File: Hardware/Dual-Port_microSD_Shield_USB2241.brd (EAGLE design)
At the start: 22.9 x 58.4 mm, 85 parts, among them IC1 USB224X_2241, J2 MICRO-SD-PUSH-PUSH-EXT-PIN, J3 AVR_SPI_PROG_3X2TESTPOINTS, J4 THING_PLUS, Q1 20V/4.2A/52mΩ/1.4W, Q2 20V/0.2A/8MHz/1.2Ω/1Vth, Q3 20V/4.2A/52mΩ/1.4W, Q4 20V/4.2A/52mΩ/1.4W, Q6 20V/4.2A/52mΩ/1.4W, U1 3.3V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

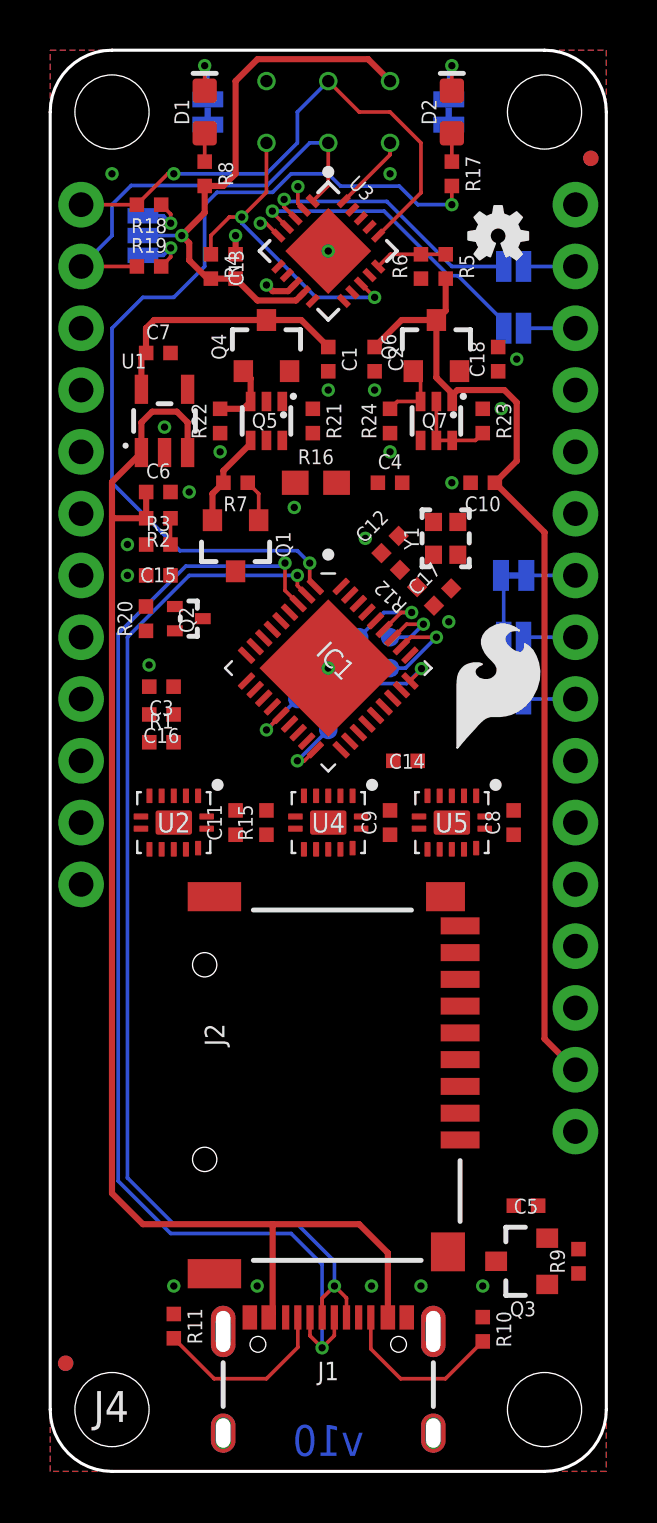
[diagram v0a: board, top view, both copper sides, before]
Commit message: Changed to 4-layer PCB. Routed. Add Schematic.pdf.
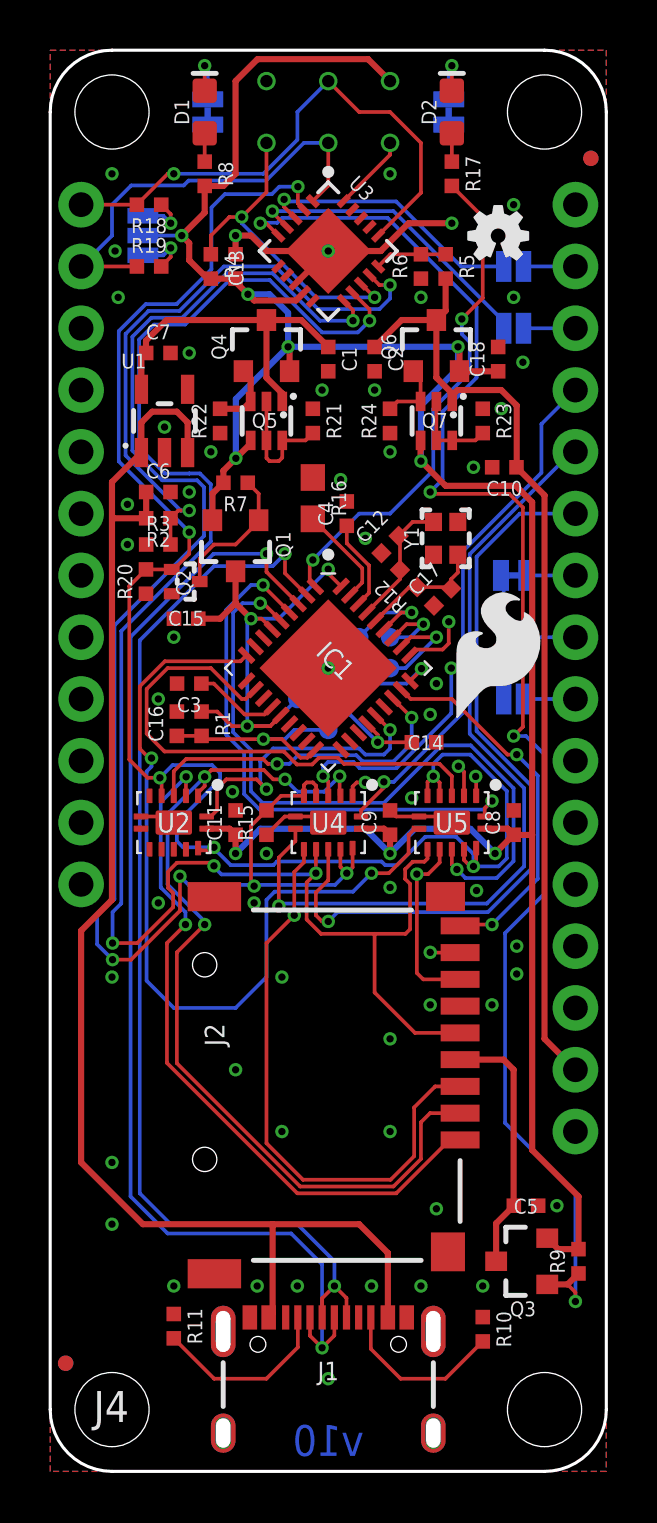
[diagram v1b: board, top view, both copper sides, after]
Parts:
- moved C4 2.18 mm to (12.2, 39.4), turned to 90 degrees
- moved C15 2.11 mm to (5.59, 35.1)
- moved R1 1.82 mm to (6.22, 30.7), turned to 270 degrees
- moved Q2 1.53 mm to (6.10, 36.6)
- moved R20 1.52 mm to (3.94, 36.6)
- moved LOGO4 1.27 mm to (18.4, 33.5)
- moved C3 1.15 mm to (5.71, 32.4)
- moved C10 1.09 mm to (18.7, 41.3)
- moved C14 1.08 mm to (15.4, 30.0)
- moved C16 0.74 mm to (5.21, 30.7), turned to 90 degrees
- moved R16 0.65 mm to (10.8, 40.0), turned to 270 degrees
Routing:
- net VCC: track 27.0 -> 110.6 mm, vias 1 -> 9
- net MICROSD_CLK/SCK: track 0.00 -> 71.0 mm, vias 0 -> 4
- net SDIO_EN: track 1.05 -> 68.5 mm, vias 1 -> 6
- net SPI_EN: track 0.00 -> 62.9 mm, vias 0 -> 5
- net MICROSD_PWR_EN: track 0.95 -> 61.7 mm, vias 1 -> 4
- net MICROSD_CMD/SDI: track 0.00 -> 38.1 mm, vias 0 -> 2
- net MICROSD_D3/!CS!: track 0.00 -> 37.4 mm, vias 0 -> 4
- net SD_CLK: track 0.00 -> 34.4 mm, vias 0 -> 2
- net PICO: track 0.00 -> 34.1 mm, vias 0 -> 1
- net SCLK: track 0.00 -> 31.3 mm, vias 0 -> 1
- net SD_D0: track 0.00 -> 29.5 mm, vias 0 -> 2
- net MICROSD_D2: track 0.00 -> 28.9 mm, vias 0 -> 2
- net SDIO_VDD: track 2.64 -> 27.1 mm, vias 1 -> 4
- net V_USB_DIV_2: track 1.08 -> 25.0 mm, vias 0 -> 2
- net SD_D1: track 0.00 -> 22.7 mm, vias 0 -> 2
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- added copper zone on layer 2, net GND
- added copper zone on layer 15, net VCC
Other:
- board text added: "4-Layer Board 1.6mm Thickness 1oz Copper (Outer layers) HASL Finish"
- board text removed: "2-Layer Board 1.6mm Thickness 1oz Copper (Outer layers) HASL Finish"

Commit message: Add silk. Replace xtal caps with calculated values. Finishing touches...
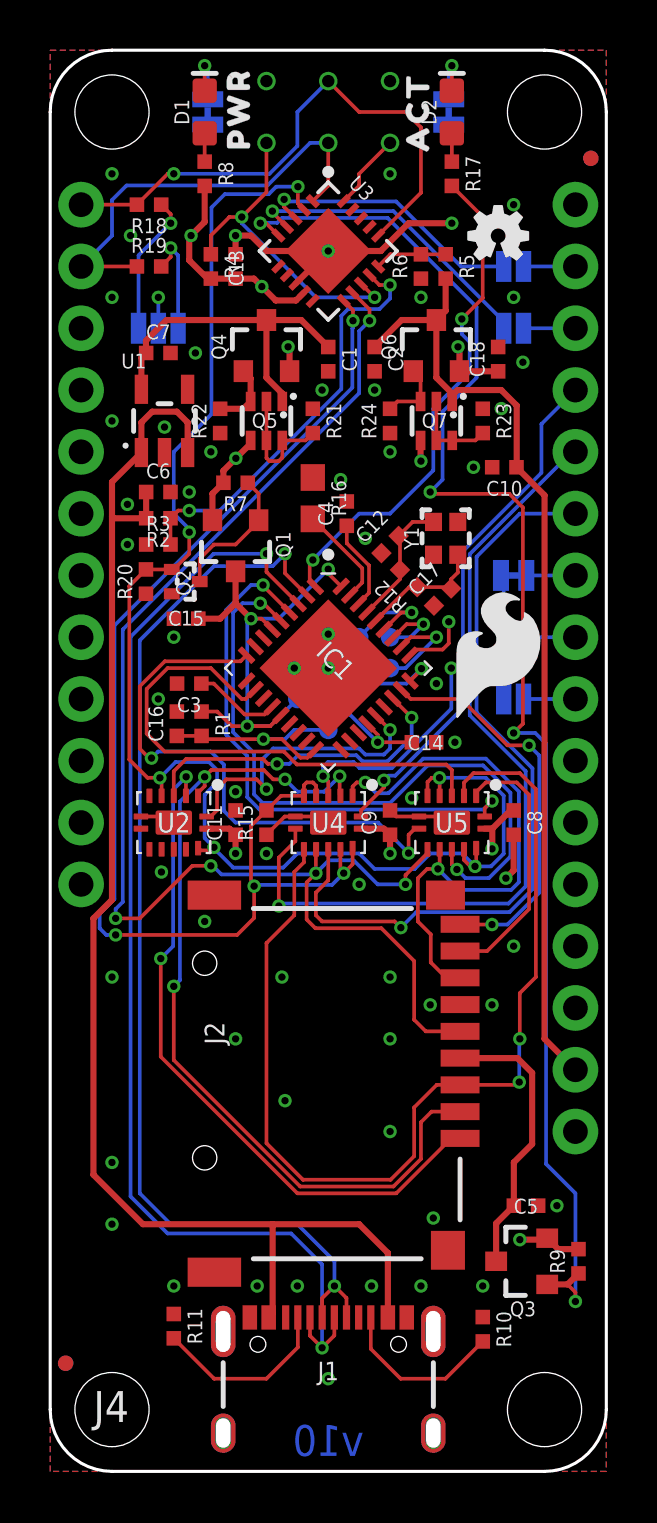
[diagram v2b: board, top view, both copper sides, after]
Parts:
- added U$1: (no value), output:#SDA#0
- added U$10: (no value), output:#TXD#0
- added U$11: (no value), output:PWR0
- added U$12: (no value), output:ACT0
- added U$13: (no value), output:#I�C#0
- added U$14: (no value), output:DUAL#PORT_MICROSD_SHIELD0
- added U$15: (no value), output:#PWR#0
- added U$16: (no value), output:#ACT#0
- added U$17: (no value), output:##CS##0
- added U$2: (no value), output:#SCL#0
- added U$3: (no value), output:#POCI#0
- added U$4: (no value), output:#PICO#0
- added U$5: (no value), output:#SCK#0
- added U$7: (no value), output:#GND#0
- added U$8: (no value), output:#3V3#0
- added U$9: (no value), output:#RXD#0
- C12, C17: value 15pF -> 12pF
- LOGO5: value SFE_LOGO_NAME_FLAME.2_INCH -> SFE_LOGO_NAME_FLAME.1_INCH; device SparkFun-Aesthetics:SFE_LOGO_NAME_FLAME_.2 -> SparkFun-Aesthetics:SFE_LOGO_NAME_FLAME_.1
- R4: value 4.7k -> 10k
- moved LOGO5 31.2 mm to (11.4, 11.2), turned to 0 degrees
- moved LOGO3 21.7 mm to (11.4, 26.7), turned to 0 degrees
- moved FRAME1 8.03 mm to (64.8, -2.54)
- moved LOGO1 8.03 mm to (34.3, 58.4)
- moved I2C 3.86 mm to (4.45, 47.0), turned to 180 degrees
- moved J2 0.06 mm to (6.35, 15.9)
- turned C8 to 270 degrees
- renumbered RX to TXD, TX to RXD
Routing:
- net VCC: track 110.6 -> 27.7 mm, vias 9 -> 11
- net MICROSD_CLK/SCK: track 71.0 -> 58.4 mm, vias 4 -> 5
- net SPI_EN: track 62.9 -> 51.1 mm, vias 5 -> 4
- net SD_CLK: track 34.4 -> 22.9 mm
- net MICROSD_D0/SDO: track 13.3 -> 23.1 mm
- net V_USB_DIV_2: track 25.0 -> 17.2 mm
- net SDIO_EN: track 68.5 -> 62.1 mm
- net MICROSD_CMD/SDI: track 38.1 -> 42.8 mm
- net N$16: track 2.19 -> 5.79 mm
- net N$14: track 2.19 -> 4.35 mm
- net GND: track 23.4 -> 25.3 mm, vias 58 -> 61
- net SD_D0: track 29.5 -> 28.3 mm
- net MICROSD_D3/!CS!: track 37.4 -> 36.3 mm
- net MICROSD_PWR_EN: track 61.7 -> 60.6 mm
- net MICROSD_VCC: track 10.6 -> 11.6 mm
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
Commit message: Corrected 74HC4066 footprint. Swapped U4 and U5.
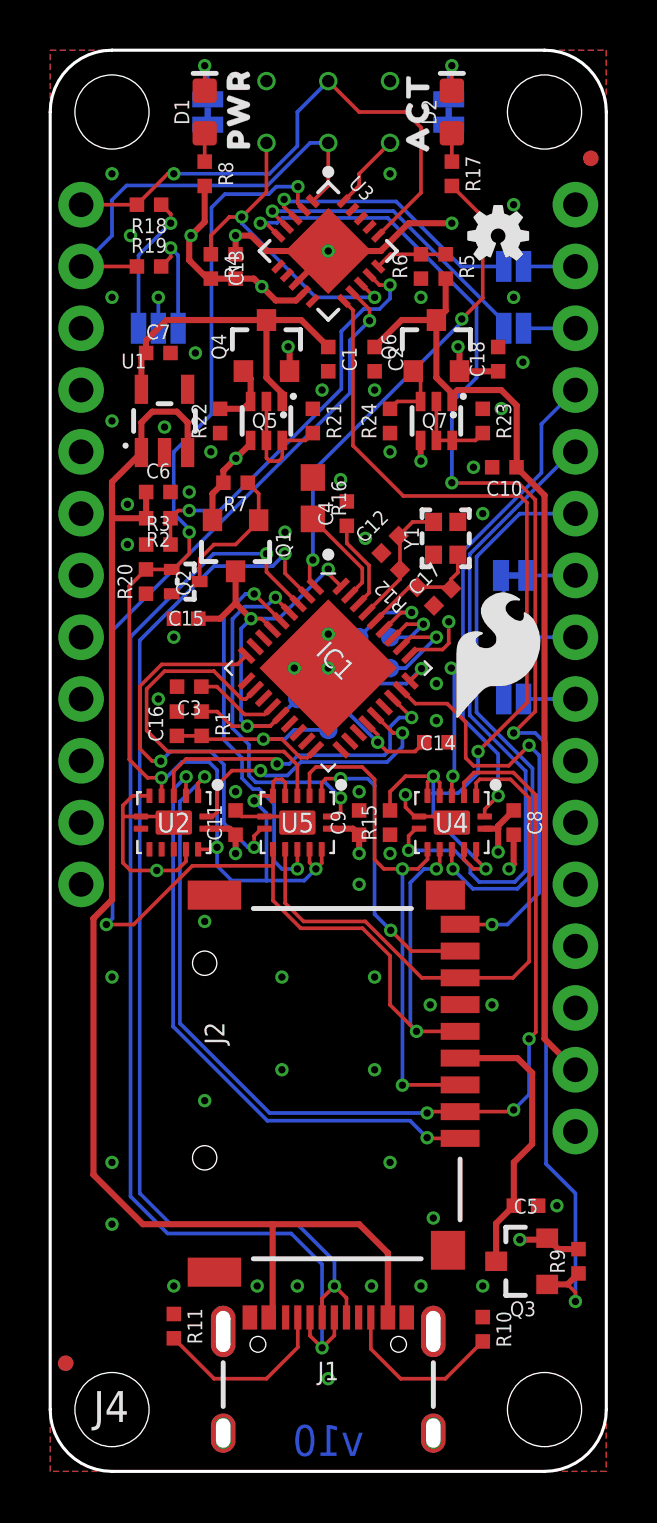
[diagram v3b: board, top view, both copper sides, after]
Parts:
- moved U5 6.35 mm to (10.2, 26.7)
- moved U4 5.08 mm to (16.5, 26.7)
- moved R15 5.08 mm to (14.0, 26.7)
- moved C9 1.27 mm to (12.7, 26.7)
- moved C14 0.51 mm to (15.9, 30.0)
- moved C3 0.13 mm to (5.71, 32.3)
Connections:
- net N$20 renamed GPIO4
- net N$21 renamed GPIO7
- net N$24 renamed SD_WP
- net N$6 renamed SDIO_!RESET!
- net N$8 renamed GPIO2
- net GND: now also U2.12, U2.6
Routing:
- net MICROSD_CMD/SDI: track 42.8 -> 21.4 mm
- net SD_D0: track 28.3 -> 16.2 mm
- net SPI_EN: track 51.1 -> 40.1 mm, vias 4 -> 3
- net GND: track 25.3 -> 35.1 mm, vias 61 -> 63
- net SDIO_EN: track 62.1 -> 52.5 mm
- net SCLK: track 32.1 -> 23.5 mm
- net MICROSD_D3/!CS!: track 36.3 -> 44.1 mm
- net SD_D1: track 22.7 -> 14.9 mm
- net PICO: track 34.6 -> 26.9 mm
- net SD_CMD: track 21.6 -> 15.2 mm
- net SD_CLK: track 22.9 -> 16.6 mm
- net !CS!: track 16.7 -> 12.6 mm
- net MICROSD_D2: track 28.3 -> 25.0 mm
- net MICROSD_CLK/SCK: track 58.4 -> 60.2 mm, vias 5 -> 4
- net SD_!CD!: track 16.2 -> 17.8 mm
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
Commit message: Add footprint for optional I2C EEPROM
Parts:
- removed GPIO2, GPIO4, GPIO7: TEST-POINT3, SparkFun-Connectors:PAD.03X.03
- added C19: 0.1uF, SparkFun-Capacitors:0402-TIGHT
- added GPIO10: TEST-POINT3, SparkFun-Connectors:PAD.03X.03
- added R13, R14, R25: 10k, SparkFun-Resistors:0402-TIGHT
- added U6: 24C04, SparkFun-IC-Memory:SO08
- moved LOGO2 19.0 mm to (18.4, 31.8)
- moved LOGO4 16.8 mm to (18.7, 50.3)
- moved SDIO_!RESET! 1.27 mm to (10.2, 30.5)
- moved C4 0.77 mm to (11.4, 39.2)
- moved R16 0.65 mm to (10.2, 39.9)
- turned R24 to 270 degrees
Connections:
- new net GPIO10: GPIO10.1, IC1.21
- net GND: now also C19.2, R25.2, U6.1, U6.2, U6.3, U6.4, U6.7
- net GPIO2: now also R13.2, U6.5; no longer GPIO2.1
- net GPIO4: now also R25.1; no longer GPIO4.1
- net GPIO7: now also R14.2, U6.6; no longer GPIO7.1
- net SDIO_VDD: now also C19.1, R13.1, R14.1, U6.8
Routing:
- net GPIO2: track 3.78 -> 17.5 mm, vias 1 -> 2
- net GPIO7: track 4.00 -> 14.4 mm, vias 1 -> 2
- net SDIO_VDD: track 28.1 -> 36.8 mm, vias 4 -> 5
- net GND: track 35.1 -> 42.2 mm, vias 63 -> 69
- net GPIO10: track 0.00 -> 3.33 mm, vias 0 -> 1
- net MICROSD_CLK/SCK: track 60.2 -> 62.5 mm
- net V_USB_DIV_2: track 16.8 -> 18.4 mm
- net SD_D2: track 13.6 -> 15.2 mm
- net ACTIVITY: track 20.0 -> 21.4 mm
- net D+: track 45.4 -> 44.1 mm
- net SDIO_!RESET!: track 9.02 -> 7.75 mm
- net SD_D3: track 12.0 -> 13.1 mm
- net VCC: track 28.0 -> 29.0 mm
- net GPIO4: track 4.03 -> 3.08 mm, vias 1 -> 0
- net N$23: track 4.18 -> 5.03 mm
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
